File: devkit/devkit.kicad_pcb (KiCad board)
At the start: 2 copper layers, 98.7 x 98.7 mm, 88 parts, among them J1 Micro_SD_Card, J10 Conn_01x04, J11 Conn_Coaxial, J12 Conn_01x22, J13 Conn_01x22, J14 Conn_01x20, J15 Conn_01x20, J16 Conn_01x03, J2 Conn_01x03, J3 Conn_01x04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

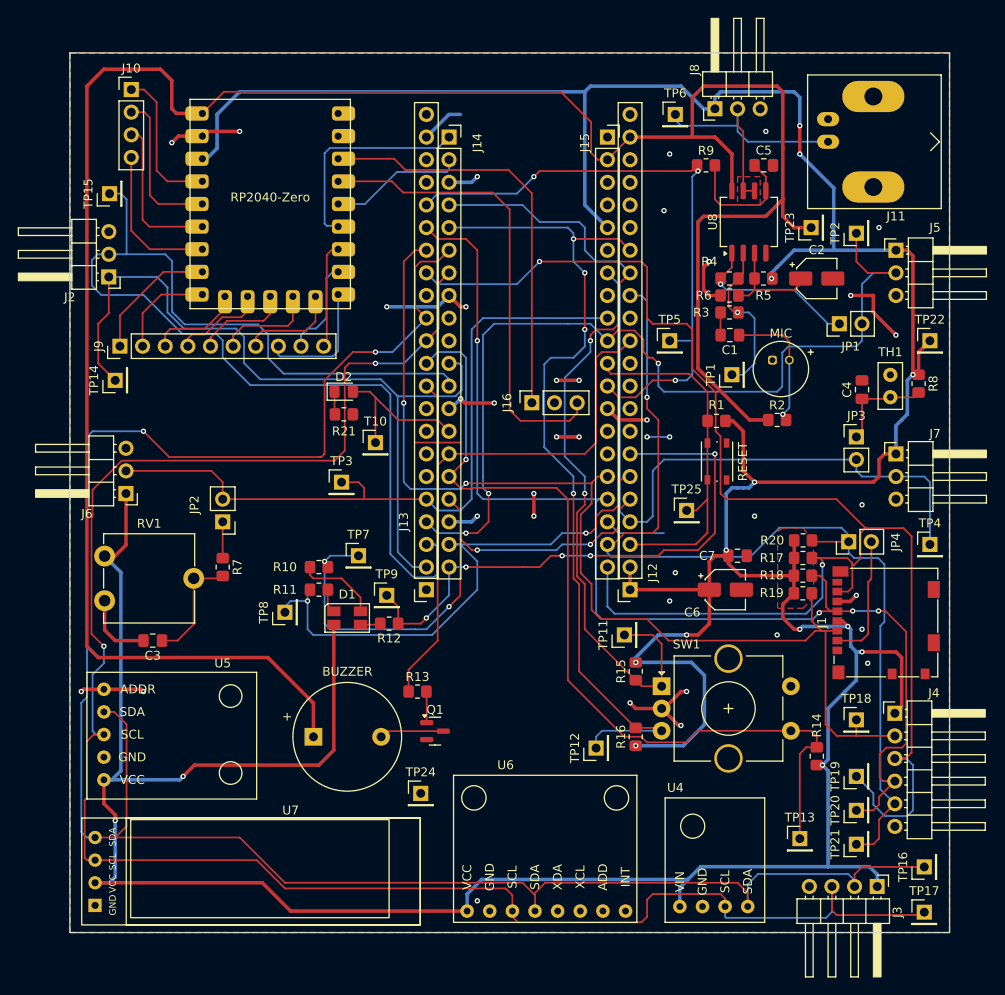
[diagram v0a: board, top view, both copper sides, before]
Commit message: chore: actualizo algunas huellas e info en pcb
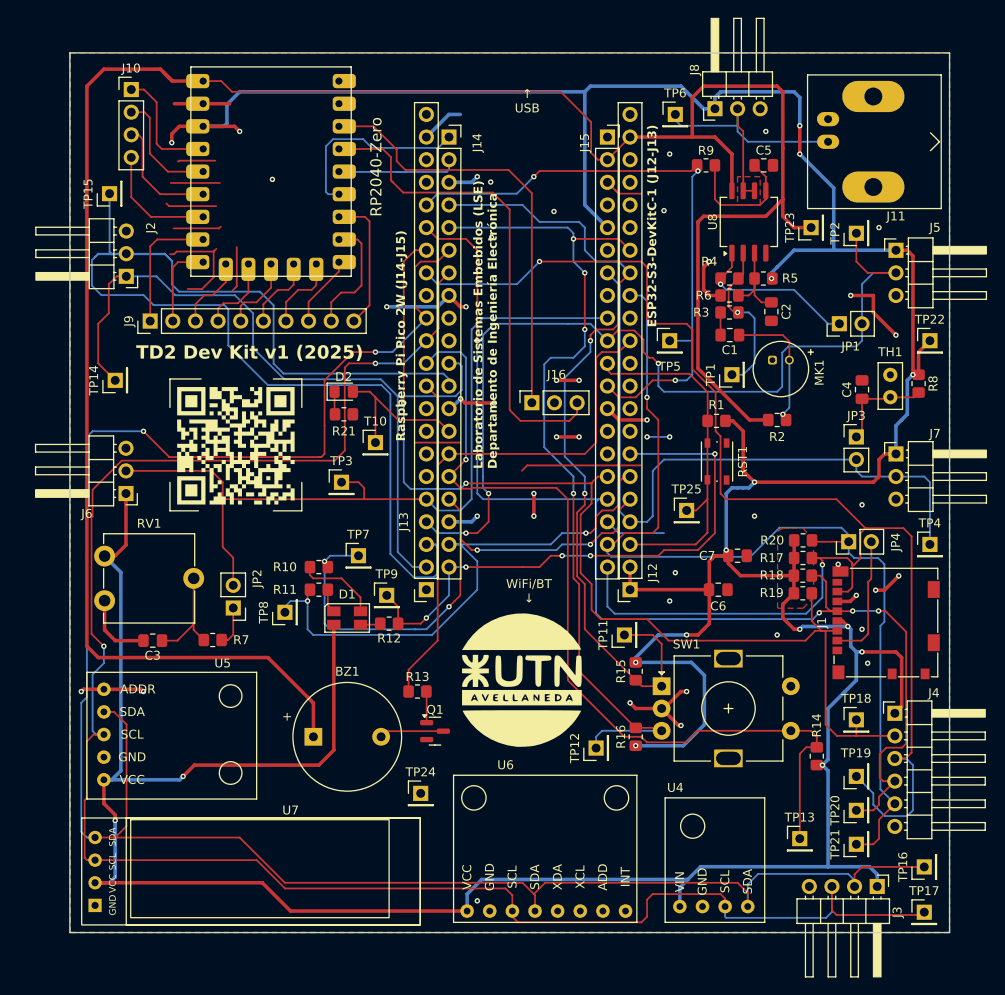
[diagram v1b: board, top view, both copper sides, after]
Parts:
- added G***: LOGO, images:qr, F.Cu at (59.9, 79.1)
- added G***: LOGO, images:utn_logo, F.Cu at (92.0, 105.4)
- C2, C6: footprint Capacitor_SMD:CP_Elec_4x5.8 -> Capacitor_SMD:C_0805_2012Metric_Pad1.18x1.45mm_HandSolder
- SW1: footprint Rotary_Encoder:RotaryEncoder_Alps_EC11E-Switch_Vertical_H20mm_CircularMountingHoles -> Rotary_Encoder:RotaryEncoder_Alps_EC11E-Switch_Vertical_H20mm
- moved JP2 9.74 mm to (59.6, 97.3)
- moved R7 8.27 mm to (57.3, 100.9), turned to 180 degrees
- moved C2 6.30 mm to (120.0, 64.0), turned to -90 degrees
- moved J9 4.41 mm to (50.3, 65.1)
- moved U3 3.64 mm to (53.7, 61.0)
- moved J2 1.97 mm to (47.6, 60.1)
- moved C6 0.79 mm to (114.0, 95.2)
- renumbered BUZZER to BZ1, MIC to MK1, RESET to RST1
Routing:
- net GND: track 104.4 -> 162.8 mm, vias 38 -> 43
- net /ADC_1: track 81.2 -> 91.5 mm
- net /UART_RX: track 131.5 -> 140.8 mm
- net +3.3V: track 504.2 -> 510.8 mm, vias 15 -> 17
- net Net-(J9-Pin_8): track 14.3 -> 8.15 mm
- net Net-(J10-Pin_3): track 17.6 -> 13.3 mm
- net Net-(J10-Pin_2): track 17.4 -> 13.2 mm
- net Net-(J9-Pin_10): track 11.9 -> 16.0 mm
- net Net-(J10-Pin_4): track 17.3 -> 13.4 mm
- net Net-(J10-Pin_1): track 16.7 -> 13.6 mm
- net /SWDIO: track 52.7 -> 55.7 mm
- net +5V: track 254.5 -> 251.7 mm
- net Net-(J9-Pin_6): track 11.3 -> 8.52 mm
- net Net-(J9-Pin_9): track 11.0 -> 13.7 mm
- net Net-(J9-Pin_7): track 11.2 -> 8.69 mm
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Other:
- board text added: "3V3"
- board text added: "5V"
- board text added: "ADC0"
- board text added: "ADC1"
- board text added: "ADC2"
- board text added: "AREF"
- board text added: "CS"
- board text added: "DAC"
- board text added: "EN"
- board text added: "ESP32-S3-DevKitC-1 (J12-J13)"
- board text added: "G"
- board text added: "GND"
- board text added: "GP0"
- board text added: "GP1"
- board text added: "GP10"
- board text added: "GP11"
- board text added: "GP12"
- board text added: "GP13"
- board text added: "GP14"
- board text added: "GP15"
- board text added: "GP16"
- board text added: "GP17"
- board text added: "GP18"
- board text added: "GP19"
- board text added: "GP2"
- board text added: "GP20"
- board text added: "GP21"
- board text added: "GP22"
- board text added: "GP26"
- board text added: "GP27"
- board text added: "GP28"
- board text added: "GP29"
- board text added: "GP3"
- board text added: "GP35"
- board text added: "GP36"
- board text added: "GP37"
- board text added: "GP38"
- board text added: "GP39"
- board text added: "GP4"
- board text added: "GP40"
- board text added: "GP41"
- board text added: "GP42"
- board text added: "GP43"
- board text added: "GP44"
- board text added: "GP45"
- board text added: "GP46"
- board text added: "GP47"
- board text added: "GP48"
- board text added: "GP5"
- board text added: "GP6"
- board text added: "GP7"
- board text added: "GP8"
- board text added: "GP9"
- board text added: "Laboratorio de Sistemas Embebidos (LSE) Departamento de Ingeniería Electrónica"
- board text added: "MISO"
- board text added: "MOSI"
- board text added: "RST"
- board text added: "RX"
- board text added: "Raspberry Pi Pico 2W (J14-J15)"
- board text added: "SCK"
- board text added: "SCL"
- board text added: "SDA"
- board text added: "SWCLK"
- board text added: "SWDIO"
- board text added: "TD2 Dev Kit v1 (2025)"
- board text added: "TX"
- board text added: "VBUS"
- board text added: "WiFi/BT ↓"
- board text added: "↑ USB"

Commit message: feat: adicion de memoria flash
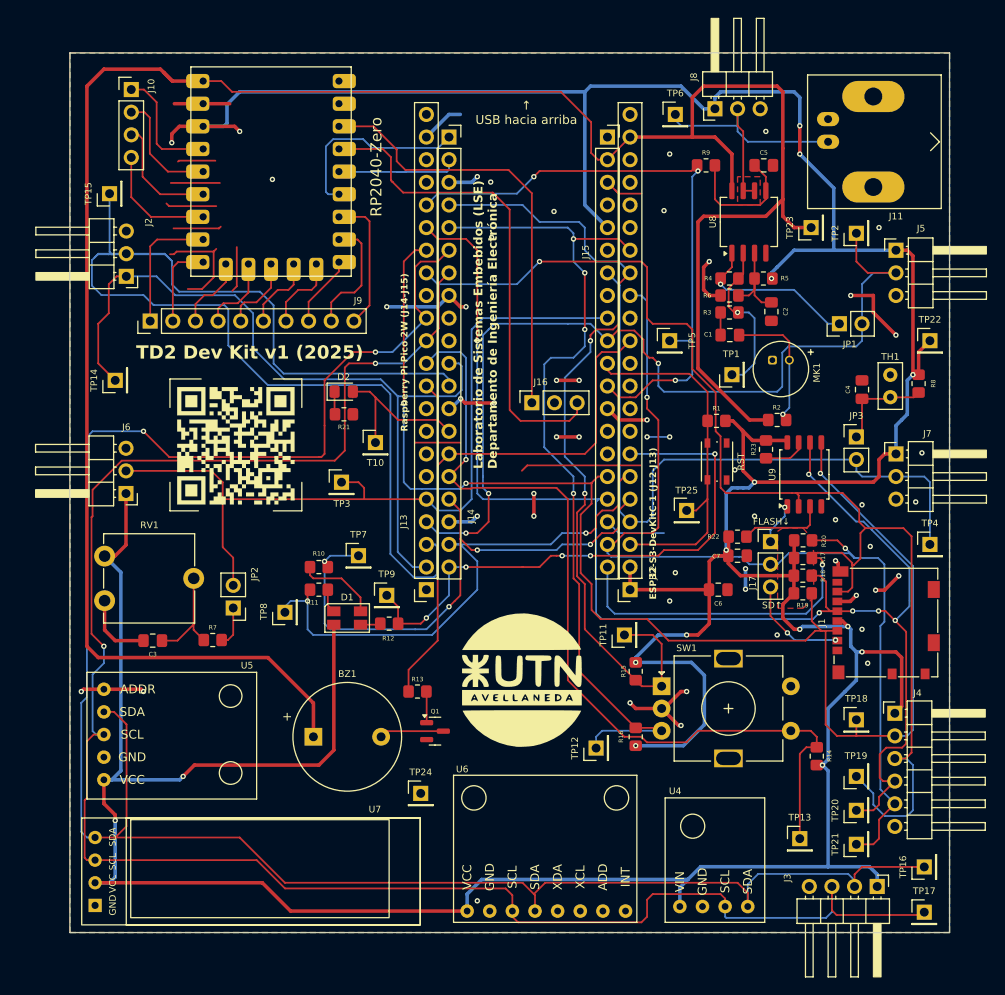
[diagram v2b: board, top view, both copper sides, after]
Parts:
- removed JP4: Jumper_2_Small_Bridged, Connector_PinHeader_2.54mm:PinHeader_1x02_P2.54mm_Vertical
- added J17: Conn_01x03, Connector_PinHeader_2.54mm:PinHeader_1x03_P2.54mm_Vertical, F.Cu at (119.9, 89.9)
- added R22: 10k, Resistor_SMD:R_0805_2012Metric_Pad1.20x1.40mm_HandSolder, F.Cu at (116.2, 89.3)
- added R23: 10k, Resistor_SMD:R_0805_2012Metric_Pad1.20x1.40mm_HandSolder, F.Cu at (119.4, 79.5)
- added U9: W25Q128JVS, Package_SO:SOIC-8_5.3x5.3mm_P1.27mm, F.Cu at (123.7, 82.3)
- renumbered RST1 to RST
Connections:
- J1 pad 10: (no net) -> GND
- J1 pad 11: (no net) -> GND
- J1 pad 2: Net-(J1-DAT3/CD) -> /Serial Interfaces/SPI_CS_SD
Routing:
- net /SPI_MOSI: track 121.7 -> 160.6 mm, vias 2 -> 3
- net /SPI_SCK: track 132.2 -> 158.0 mm, vias 4 -> 6
- net /Serial Interfaces/SPI_CS_SD: track 0.00 -> 15.1 mm, vias 0 -> 2
- net Net-(J1-DAT3/CD): track 14.3 -> 0.00 mm
- net Net-(U9-~{WP}/IO_{2}): track 0.00 -> 9.75 mm
- net +3.3V: track 510.8 -> 518.6 mm
- net Net-(U9-~{HOLD}/~{RESET}/IO_{3}): track 0.00 -> 4.88 mm
- net /Serial Interfaces/SPI_CS_FLASH: track 0.00 -> 4.86 mm, vias 0 -> 1
- net GND: track 162.8 -> 165.7 mm, vias 43 -> 50
- net /SPI_MISO: track 173.5 -> 176.0 mm
- net /SPI_CS: track 110.4 -> 109.6 mm, vias 1 -> 2
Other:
- board text added: "FLASH↓"
- board text added: "SD↑"
- board text added: "↑ USB hacia arriba"
- board text removed: "WiFi/BT ↓"
- board text removed: "↑ USB"

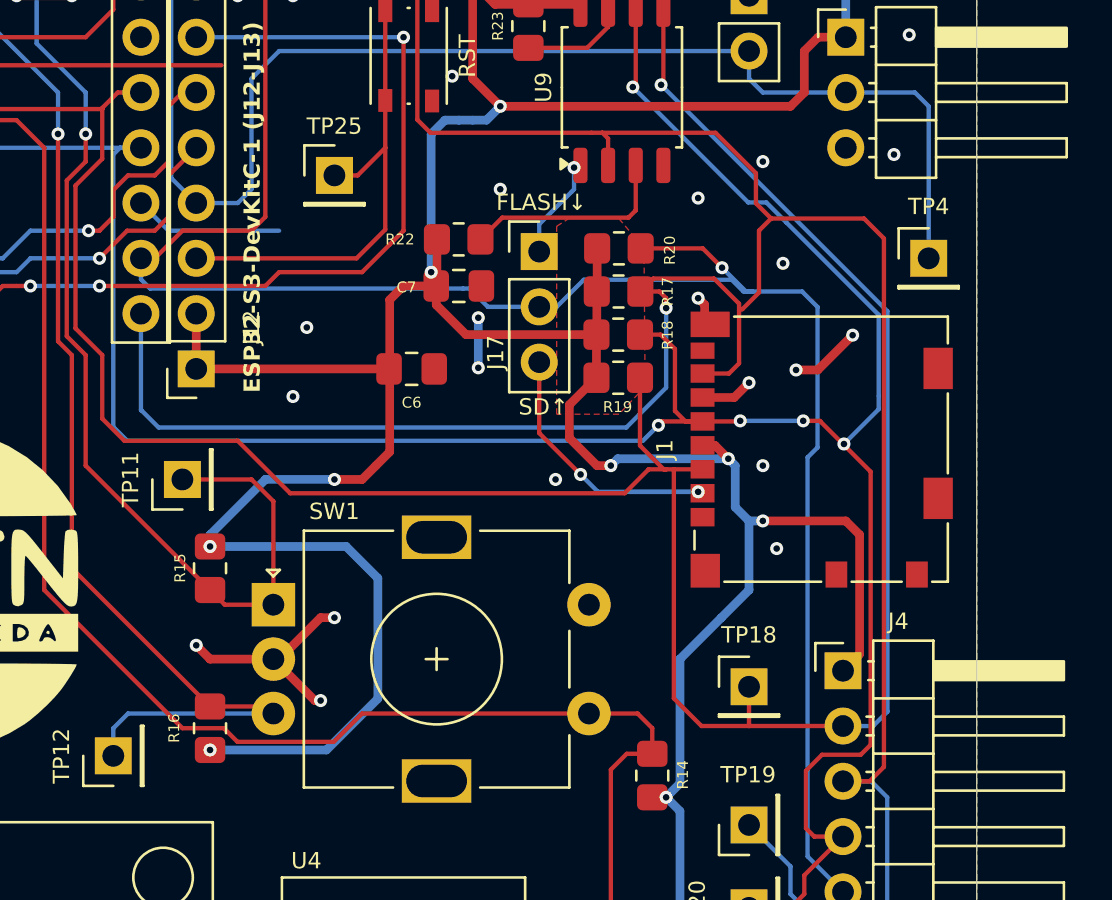
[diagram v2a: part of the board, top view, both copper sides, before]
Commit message: fix: fix sd connector orientation
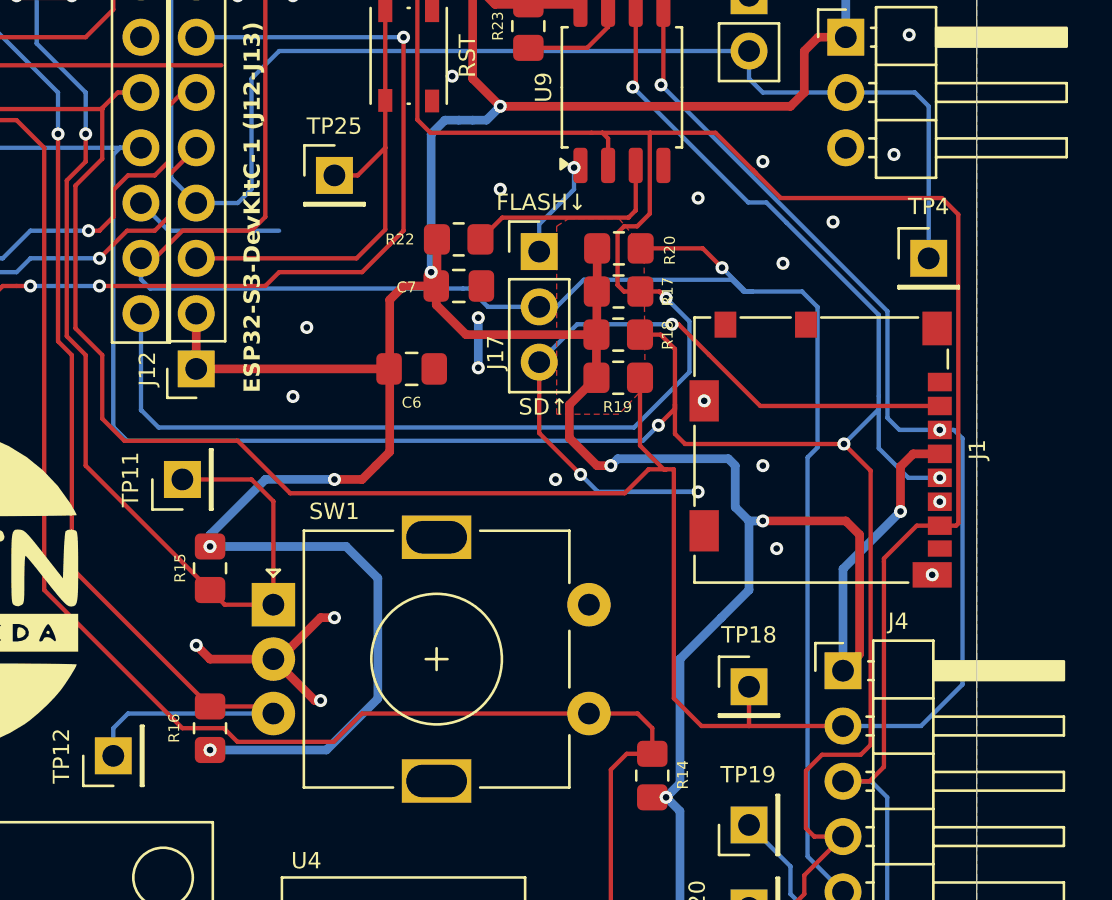
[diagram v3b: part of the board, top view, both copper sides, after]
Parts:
- turned J1 to -90 degrees
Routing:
- net /Serial Interfaces/SPI_CS_SD: track 15.1 -> 35.6 mm, vias 2 -> 3
- net +3.3V: track 518.6 -> 529.7 mm
- net GND: track 165.7 -> 158.8 mm
- net /SPI_SCK: track 158.0 -> 164.1 mm, vias 6 -> 5
- net /SPI_MOSI: track 160.6 -> 164.9 mm, vias 3 -> 4
- net /SPI_MISO: track 176.0 -> 177.4 mm
